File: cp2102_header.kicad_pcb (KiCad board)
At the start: 2 copper layers, 15.2 x 21.6 mm, 26 parts, among them J1 FTDI, J2 USB_B_Micro, Q3 BSS138PS, Q4 BSS138PS, U2 CP2102N

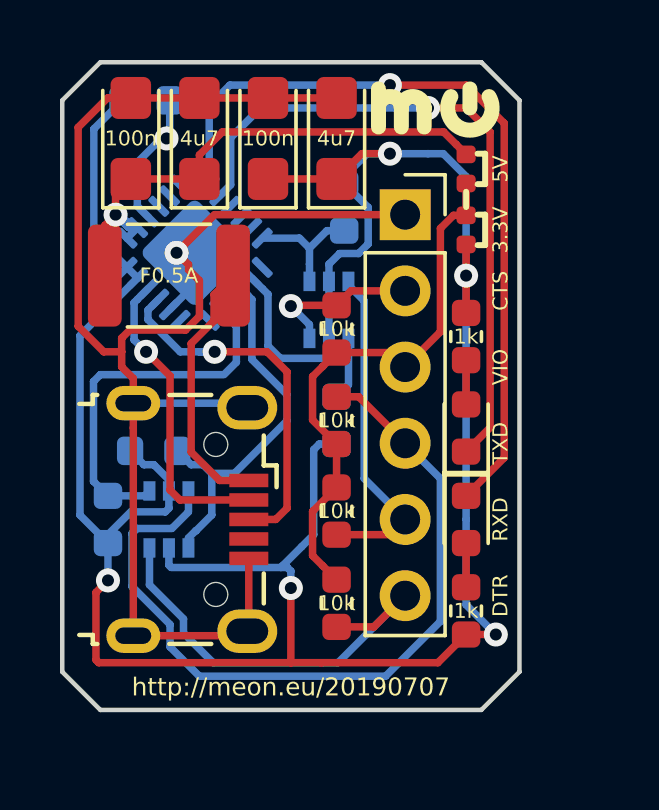
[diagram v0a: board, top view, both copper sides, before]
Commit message: usb connector can be soldered on both sides
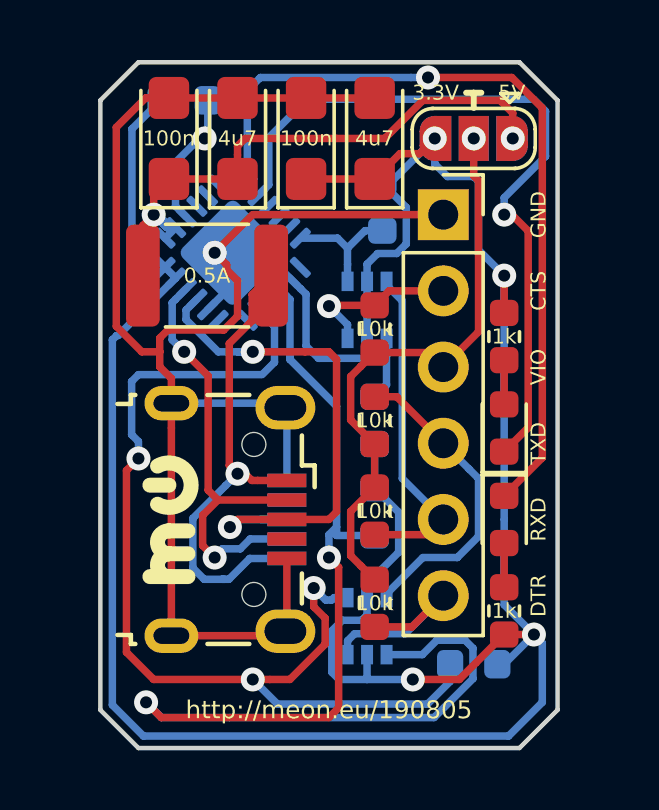
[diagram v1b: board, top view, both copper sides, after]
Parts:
- removed R93, R95: 0, Resistor_SMD:R_0402_1005Metric
- added J22: USB_B_Micro, test-footprint:USB_Micro-B_Wuerth_629105150521_usb_lines_only, B.Cu at (80.5, 86.4)
- added JP9: SJMP, Jumper:SolderJumper-3_P1.3mm_Open_RoundedPad1.0x1.5mm, F.Cu at (88.6, 73.7)
- added JP92: sjmp, Jumper:SolderJumper-3_P1.3mm_Open_RoundedPad1.0x1.5mm, B.Cu at (88.6, 73.7)
- F2: value F0.5A -> 0.5A
- moved REF** 16.3 mm to (78.5, 86.4), turned to 90 degrees
- moved R34 13.1 mm to (88.6, 91.2), turned to 0 degrees
- moved R31 7.64 mm to (85.3, 86.1), turned to 90 degrees
- moved Q3 7.50 mm to (85.1, 89.9)
- moved C22 1.27 mm to (83.1, 73.7)
- moved C23 1.27 mm to (80.8, 73.7)
- moved C24 1.27 mm to (78.5, 73.7)
- moved D21 1.27 mm to (89.7, 83.3)
- moved D22 1.27 mm to (89.7, 86.4)
- moved Q4 1.27 mm to (85.1, 79.4)
- moved R21 1.27 mm to (89.7, 80.3)
- moved R22 1.27 mm to (89.7, 89.4)
- moved C21 1.27 mm to (85.3, 73.7)
- moved F2 1.27 mm to (79.8, 78.2)
- moved J1 1.27 mm to (87.6, 76.2)
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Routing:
- net U_TXD: track 12.6 -> 39.4 mm, vias 0 -> 2
- net U_DTR: track 12.6 -> 34.9 mm, vias 0 -> 3
- net TXD: track 27.2 -> 11.0 mm
- net DTR: track 14.7 -> 6.99 mm
- net Net-(F2-Pad2): track 8.77 -> 16.5 mm, vias 0 -> 1
- net D+: track 12.4 -> 18.4 mm, vias 1 -> 2
- net +3V3: track 86.8 -> 92.6 mm, vias 5 -> 4
- net D-: track 10.2 -> 15.2 mm, vias 1 -> 2
- net GND: track 53.4 -> 55.9 mm
- net +5V: track 18.8 -> 20.9 mm, vias 1 -> 2
- net TXL: track 22.5 -> 24.5 mm
- net VIO: track 18.6 -> 19.6 mm, vias 0 -> 1
- net RXL: track 26.2 -> 26.8 mm
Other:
- board size 15.2 x 21.6 mm -> 15.2 x 22.9 mm
- board text added: "GND"
- board text added: "http://meon.eu/190805"
- board text removed: "http://meon.eu/20190707"

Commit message: add one extra pin for fixation, bigger labels, more/cleaner F/B-Silk lines
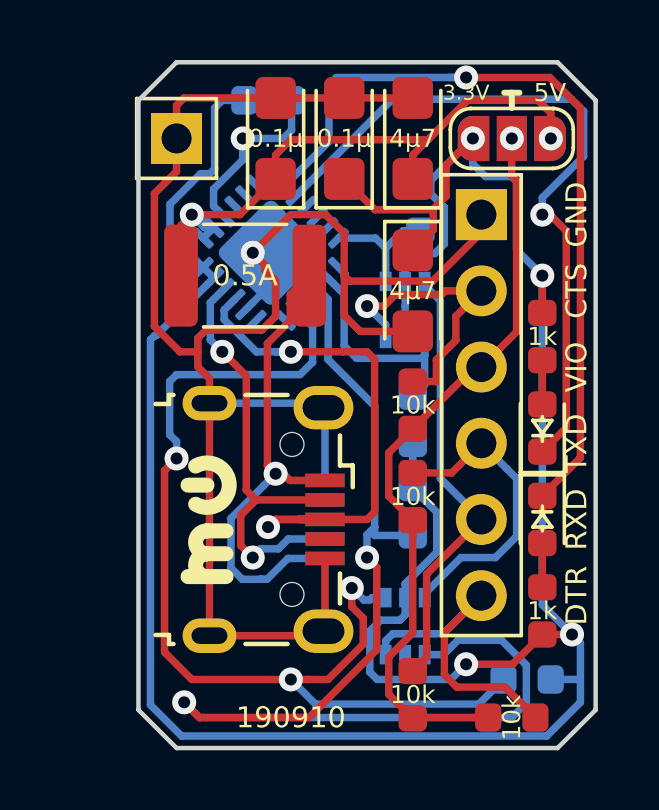
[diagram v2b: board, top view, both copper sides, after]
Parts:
- added J8: mount, Connector_PinHeader_2.54mm:PinHeader_1x01_P2.54mm_Vertical_closed, F.Cu at (78.7, 73.7)
- C21, C23: value 4u7 -> 4μ7
- C22, C24: value 100n -> 0.1μ
- D21, D22: footprint LED_SMD:LED_0603_1608Metric -> LED_SMD:LED_0603_1608Metric_symbol
- J1: footprint Connector_PinSocket_2.54mm:PinSocket_1x06_P2.54mm_Vertical -> Connector_PinSocket_2.54mm:PinSocket_1x06_P2.54mm_Vertical_closed
- JP9, JP92: footprint Jumper:SolderJumper-3_P1.3mm_Open_RoundedPad1.0x1.5mm -> Jumper (GitHub):SolderJumper-3_P1.3mm_Open_RoundedPad1.0x1.5mm_no_arrow
- Q3, Q4: footprint Package_TO_SOT_SMD:SOT-363_SC-70-6 -> Package_TO_SOT_SMD (GitHub):SOT-363_SC-70-6_dot
- R2, R21, R22, R31, R33, R34, R36, R41, R43, R44, R46: footprint Resistor_SMD:R_0603_1608Metric -> Resistor_SMD (GitHub):R_0603_1608Metric_no_lines
- moved R43 6.25 mm to (86.6, 92.2), turned to 270 degrees
- moved R33 5.95 mm to (89.9, 93.0), turned to 180 degrees
- moved C23 5.84 mm to (86.6, 73.7)
- moved C21 5.24 mm to (86.6, 78.7), turned to 270 degrees
- moved C24 3.56 mm to (82.0, 73.7)
- moved R36 2.84 mm to (86.6, 85.6)
- moved R46 2.84 mm to (86.6, 82.5)
- moved R2 2.79 mm to (81.8, 72.4)
- moved R34 1.85 mm to (90.4, 91.7)
- moved J1 1.27 mm to (88.9, 76.2)
- moved R31 1.27 mm to (86.6, 86.1)
- moved R44 1.27 mm to (86.6, 83.1)
- moved C22 1.27 mm to (84.3, 73.7)
- moved D21 1.27 mm to (90.9, 83.3)
- moved D22 1.27 mm to (90.9, 86.4)
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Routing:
- net GND: track 55.9 -> 62.7 mm
- net VIO: track 19.6 -> 24.8 mm
- net CTS: track 5.35 -> 9.82 mm
- net RXD: track 11.2 -> 15.4 mm
- net DTR: track 6.99 -> 11.0 mm
- net +3V3: track 92.6 -> 96.3 mm
- net Net-(R2-Pad1): track 4.77 -> 6.05 mm
- net +5V: track 20.9 -> 21.9 mm
- net TXL: track 24.5 -> 23.6 mm
- net TXD: track 11.0 -> 10.3 mm
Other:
- board text added: "190910"
- board text added: "http://meon.eu/190910"
- board text removed: "http://meon.eu/190805"

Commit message: move R around, full link on F.SilkS, bigger 2 gnd copper pads on usb from connector
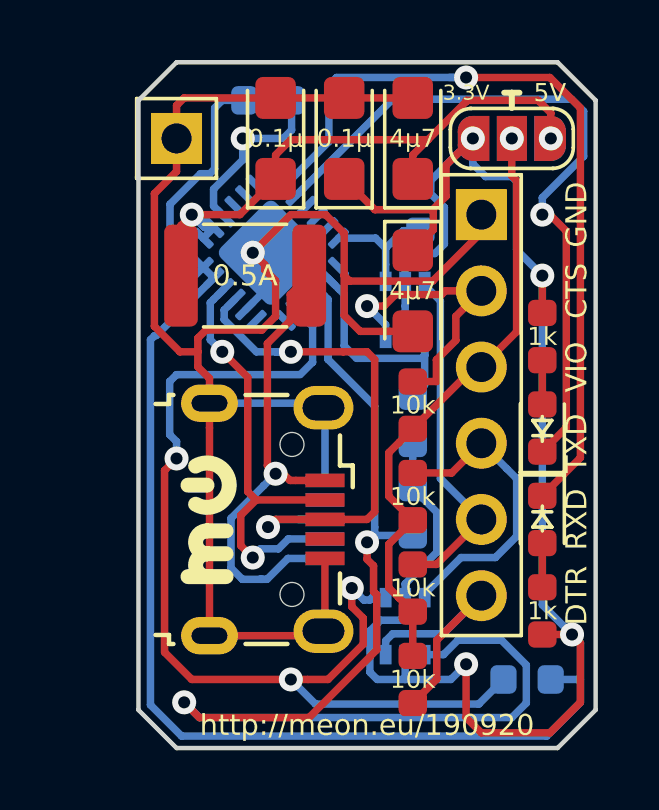
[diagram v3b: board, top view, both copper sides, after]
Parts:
- moved R43 3.56 mm to (86.6, 88.6)
- moved R33 3.54 mm to (86.6, 91.7), turned to 90 degrees
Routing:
- net +3V3: track 96.3 -> 101.9 mm
- net VIO: track 24.8 -> 20.2 mm
- net RXD: track 15.4 -> 11.6 mm
- net DTR: track 11.0 -> 8.80 mm
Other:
- board text added: "http://meon.eu/190920"
- board text removed: "190910"
- board text removed: "http://meon.eu/190910"

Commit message: tx/rx leds on both sides
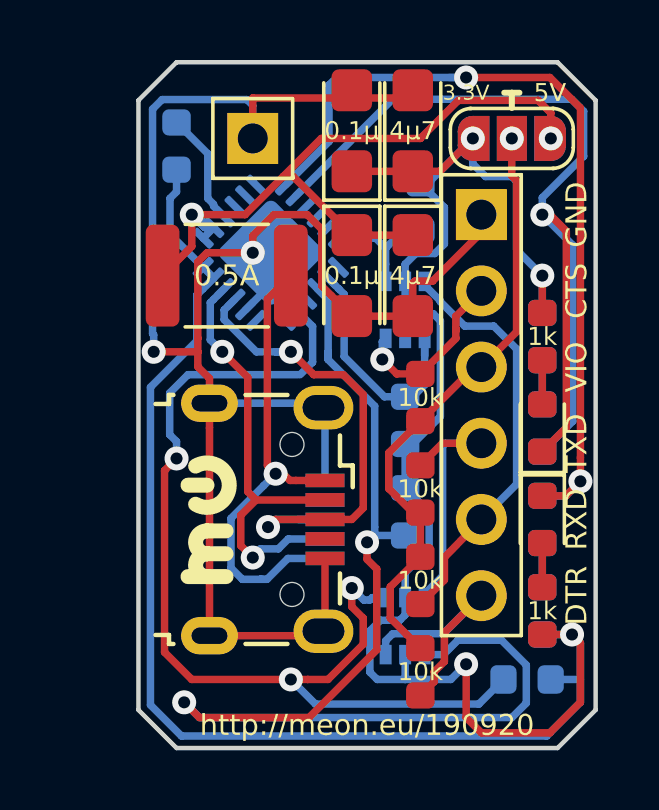
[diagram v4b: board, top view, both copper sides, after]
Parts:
- added D23: TX_LED, LED_SMD:LED_0603_1608Metric, B.Cu at (90.9, 83.3)
- added D24: RX_LED, LED_SMD:LED_0603_1608Metric, B.Cu at (90.9, 86.4)
- added R23: 1k, Resistor_SMD:R_0603_1608Metric, B.Cu at (90.9, 80.3)
- added R24: 1k, Resistor_SMD:R_0603_1608Metric, B.Cu at (90.9, 89.4)
- D21, D22: footprint LED_SMD:LED_0603_1608Metric_symbol -> LED_SMD:LED_0603_1608Metric
- moved C21 5.33 mm to (86.6, 73.4), turned to 90 degrees
- moved C24 5.23 mm to (84.6, 78.2), turned to 270 degrees
- moved C23 4.57 mm to (86.6, 78.2), turned to 270 degrees
- moved R2 3.41 mm to (78.7, 73.9), turned to 270 degrees
- moved J8 2.54 mm to (81.3, 73.7)
- moved F2 0.61 mm to (80.4, 78.2)
- moved R33 0.36 mm to (86.9, 91.4)
- moved R36 0.36 mm to (86.9, 85.3)
- moved R43 0.36 mm to (86.9, 88.4), turned to 90 degrees
- moved C22 0.36 mm to (84.6, 73.4)
- moved R46 0.36 mm to (86.9, 82.3)
- moved R31 0.25 mm to (86.4, 86.1)
- moved R44 0.25 mm to (86.4, 83.1)
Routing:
- net +3V3: track 101.9 -> 90.4 mm
- net TXL: track 23.6 -> 32.3 mm
- net CTS: track 9.82 -> 5.89 mm
- net +5V: track 21.9 -> 25.2 mm
- net RXD: track 11.6 -> 13.9 mm
- net Net-(R2-Pad1): track 6.05 -> 3.81 mm, vias 1 -> 0
- net RXL: track 26.6 -> 28.5 mm, vias 1 -> 2
- net GND: track 62.7 -> 64.3 mm, vias 1 -> 2
- net D+: track 18.4 -> 16.9 mm
- net Net-(D24-Pad2): track 0.00 -> 1.47 mm
- net Net-(D23-Pad2): track 0.00 -> 1.47 mm
- net TXD: track 10.3 -> 8.97 mm

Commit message: round mounting hole, add more SilkS lines
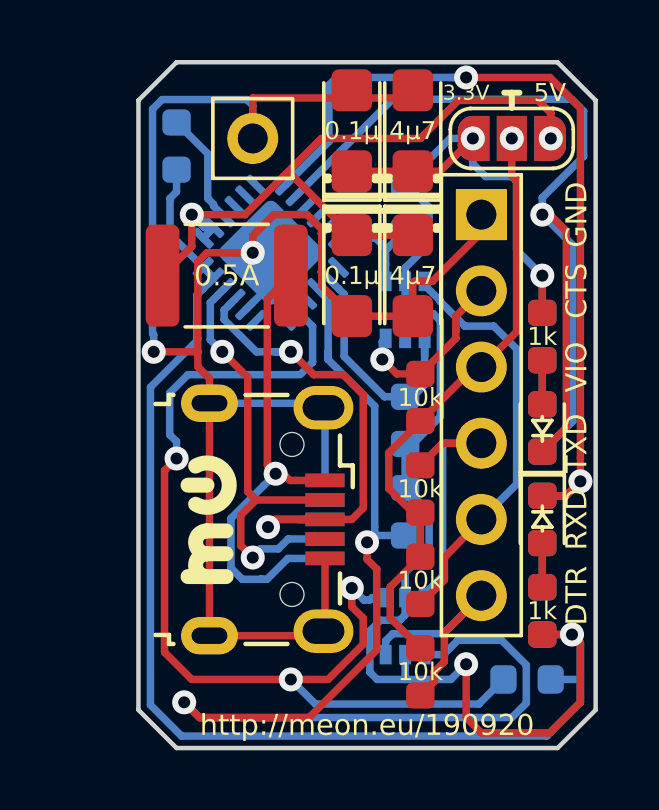
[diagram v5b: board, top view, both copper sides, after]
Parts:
- D21, D22, D23, D24: footprint LED_SMD:LED_0603_1608Metric -> LED_SMD.debian:LED_0603_1608Metric_symbol
- moved R41 0.51 mm to (86.4, 75.9)
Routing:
- net U_CTS: track 4.22 -> 3.71 mm

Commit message: tracks clean-up
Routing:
- net +5V: track 25.2 -> 24.7 mm
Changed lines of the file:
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@@
     (thickness 1.6)
     (drawings 47)
-    (tracks 365)
+    (tracks 362)
     (zones 0)
     (modules 32)
@@
   (segment (start 84.074 72.056) (end 84.328 72.31) (width 0.25) (layer F.Cu) (net 2))
   (segment (start 86.614 72.31) (end 84.328 72.31) (width 0.25) (layer F.Cu) (net 2))
-  (segment (start 81.28 72.31) (end 81.28 73.66) (width 0.25) (layer F.Cu) (net 2))
-  (segment (start 84.328 72.31) (end 81.28 72.31) (width 0.25) (layer F.Cu) (net 2))
   (via (at 77.978 80.772) (size 0.8) (drill 0.4) (layers F.Cu B.Cu) (net 2))
   (segment (start 79.45 80.772) (end 77.978 80.772) (width 0.25) (layer F.Cu) (net 2))
@@
   (segment (start 78.25801 72.36399) (end 81.08399 72.36399) (width 0.25) (layer B.Cu) (net 2))
   (segment (start 77.978 80.772) (end 77.978 80.206315) (width 0.25) (layer B.Cu) (net 2))
+  (segment (start 84.582 72.056) (end 81.741 72.056) (width 0.25) (layer F.Cu) (net 2))
+  (segment (start 81.741 72.056) (end 81.28 72.517) (width 0.25) (layer F.Cu) (net 2))
+  (segment (start 81.28 72.517) (end 81.28 73.66) (width 0.25) (layer F.Cu) (net 2))
   (segment (start 79.628598 76.983864) (end 79.982151 76.630311) (width 0.25) (layer B.Cu) (net 3))
   (segment (start 79.628597 76.983864) (end 79.628598 76.983864) (width 0.25) (layer B.Cu) (net 3))
@@
   (via (at 79.248 76.2) (size 0.8) (drill 0.4) (layers F.Cu B.Cu) (net 3))
   (via (at 91.216 73.66) (size 0.8) (drill 0.4) (layers F.Cu B.Cu) (net 3))
-  (segment (start 91.216 73.124998) (end 91.216 73.66) (width 0.25) (layer B.Cu) (net 3))
   (segment (start 79.248 77.259) (end 78.275 78.232) (width 0.25) (layer F.Cu) (net 3))
   (segment (start 79.248 76.2) (end 79.248 77.259) (width 0.25) (layer F.Cu) (net 3))
@@
   (segment (start 82.722189 79.370349) (end 83.275001 79.923161) (width 0.25) (layer B.Cu) (net 9))
   (segment (start 79.756 81.534) (end 82.804 81.534) (width 0.25) (layer B.Cu) (net 9))
-  (segment (start 85.26 88.966) (end 85.26 88.966) (width 0.25) (layer B.Cu) (net 9))
   (via (at 78.74 84.328) (size 0.8) (drill 0.4) (layers F.Cu B.Cu) (net 9))
   (segment (start 82.55 91.694) (end 79.248 91.694) (width 0.25) (layer F.Cu) (net 9))
@@
   (segment (start 78.74 83.762315) (end 78.5115 83.533815) (width 0.25) (layer B.Cu) (net 9))
   (segment (start 78.74 84.328) (end 78.74 83.762315) (width 0.25) (layer B.Cu) (net 9))
-  (segment (start 85.26 88.966) (end 85.71 88.966) (width 0.25) (layer B.Cu) (net 9))
   (via (at 84.582 88.646) (size 0.8) (drill 0.4) (layers F.Cu B.Cu) (net 9))
-  (segment (start 84.981999 89.045999) (end 84.582 88.646) (width 0.25) (layer B.Cu) (net 9))
-  (segment (start 85.180001 89.045999) (end 84.981999 89.045999) (width 0.25) (layer B.Cu) (net 9))
-  (segment (start 85.26 88.966) (end 85.180001 89.045999) (width 0.25) (layer B.Cu) (net 9))
   (segment (start 83.788938 91.694) (end 83.115685 91.694) (width 0.25) (layer F.Cu) (net 9))
   (segment (start 84.96301 90.519928) (end 83.788938 91.694) (width 0.25) (layer F.Cu) (net 9))
@@
   (segment (start 78.5115 82.142983) (end 79.120483 81.534) (width 0.25) (layer B.Cu) (net 9))
   (segment (start 78.5115 83.533815) (end 78.5115 82.142983) (width 0.25) (layer B.Cu) (net 9))
+  (segment (start 84.902 88.966) (end 84.582 88.646) (width 0.25) (layer B.Cu) (net 9))
+  (segment (start 85.71 88.966) (end 84.902 88.966) (width 0.25) (layer B.Cu) (net 9))
   (via (at 85.598 81.026) (size 0.8) (drill 0.4) (layers F.Cu B.Cu) (net 10))
   (segment (start 88.050001 79.589999) (end 88.9 78.74) (width 0.25) (layer F.Cu) (net 10))
